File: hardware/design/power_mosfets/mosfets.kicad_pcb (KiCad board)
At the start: 2 copper layers, 123 x 44 mm, 21 parts, among them Q5 IRFS3006

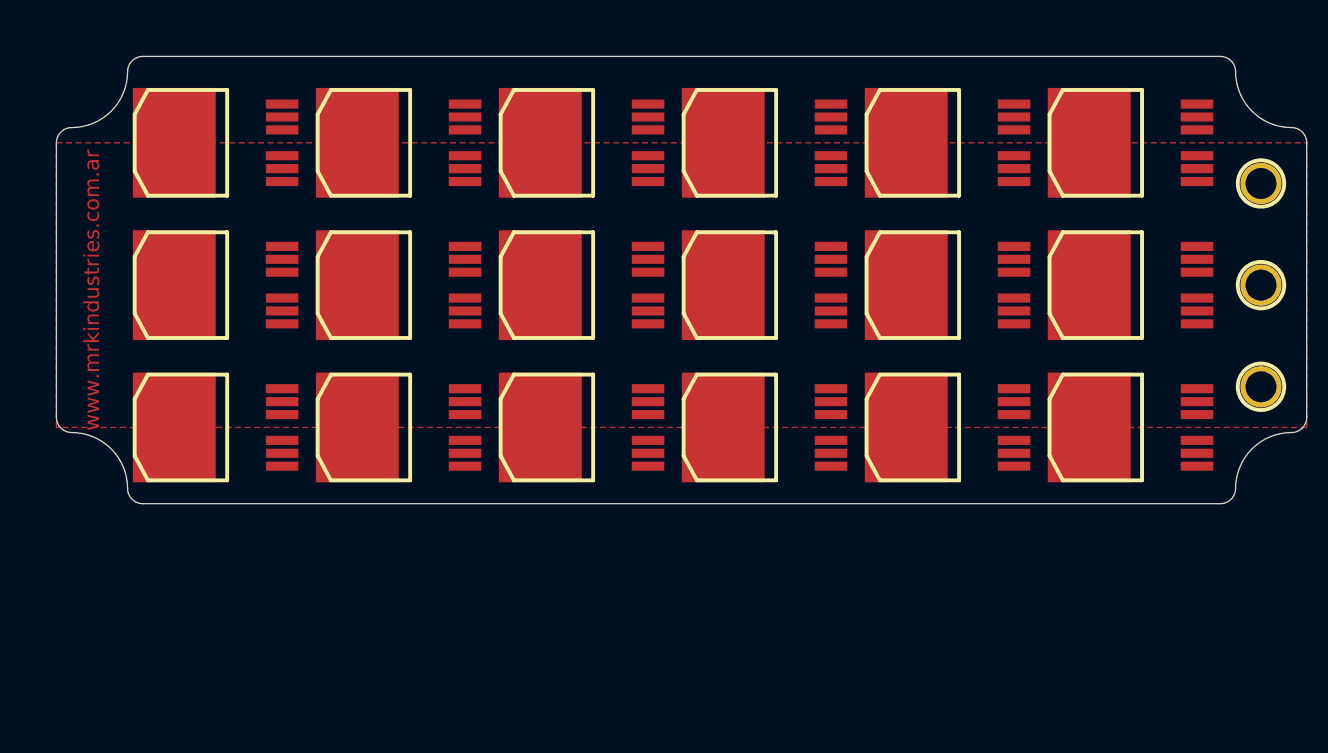
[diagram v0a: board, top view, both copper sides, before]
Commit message: Schematic changes: Cleaner top level, added CAN connector, moved LEDs to top level, added 22 Ohm resistors for the USB lines. Fully annotated schematic, ready for layout.
Signed-off-by: Marcos Chaparro <marcos@mrkindustries.com.ar>
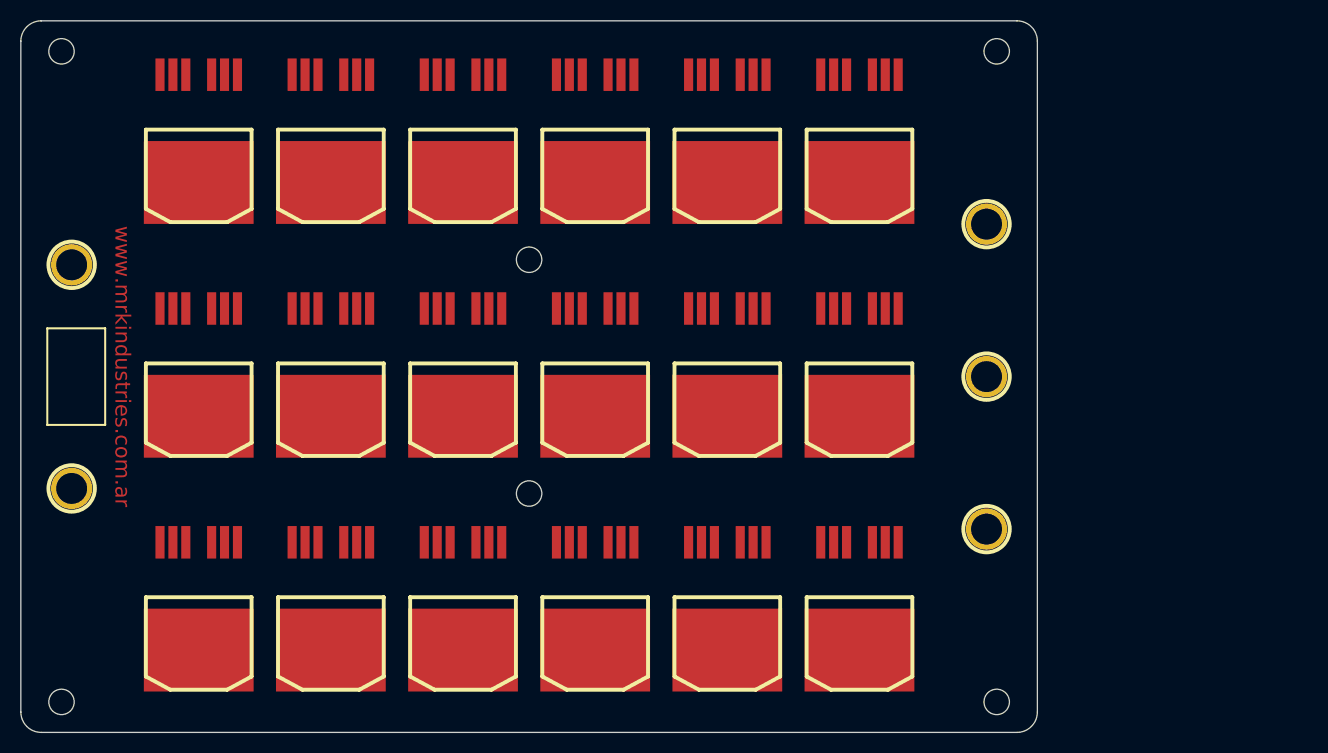
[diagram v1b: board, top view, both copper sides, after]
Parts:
- added 1PIN: P***, Connect:1pin, F.Cu at (102.0, 87.0)
- added 1PIN: P***, Connect:1pin, F.Cu at (102.0, 109.0)
- added 1PIN: P***, Connect:1pin, F.Cu at (193.0, 130.0)
- added 1PIN: P***, Connect:1pin, F.Cu at (101.0, 130.0)
- added 1PIN: P***, Connect:1pin, F.Cu at (147.0, 109.5)
- added 1PIN: P***, Connect:1pin, F.Cu at (147.0, 86.5)
- added 1PIN: P***, Connect:1pin, F.Cu at (193.0, 66.0)
- added 1PIN: P***, Connect:1pin, F.Cu at (101.0, 66.0)
- moved Q5 32.7 mm to (179.5, 119.0), turned to 180 degrees
- moved 1PIN 30.4 mm to (192.0, 113.0)
- moved Q5 29.3 mm to (179.5, 96.0), turned to 180 degrees
- moved Q5 28.6 mm to (179.5, 73.0), turned to 180 degrees
- moved 1PIN 28.5 mm to (192.0, 98.0)
- moved Q5 28.4 mm to (166.5, 119.0), turned to 180 degrees
- moved 1PIN 27.3 mm to (192.0, 83.0)
- moved Q5 24.5 mm to (166.5, 96.0), turned to 180 degrees
- moved Q5 24.5 mm to (153.5, 119.0), turned to 180 degrees
- moved Q5 23.6 mm to (166.5, 73.0), turned to 180 degrees
- moved Q5 20.9 mm to (140.5, 119.0), turned to 180 degrees
- moved Q5 19.8 mm to (153.5, 96.0), turned to 180 degrees
- moved Q5 18.6 mm to (153.5, 73.0), turned to 180 degrees
- moved Q5 18.1 mm to (127.5, 119.0), turned to 180 degrees
- moved Q5 16.4 mm to (114.5, 119.0), turned to 180 degrees
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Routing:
- removed copper zone on F.Cu, net (none)
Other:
- board size 123 x 44 mm -> 100 x 70 mm
